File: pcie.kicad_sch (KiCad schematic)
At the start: 3 parts, among them U3002 XC7K160T-FFG676

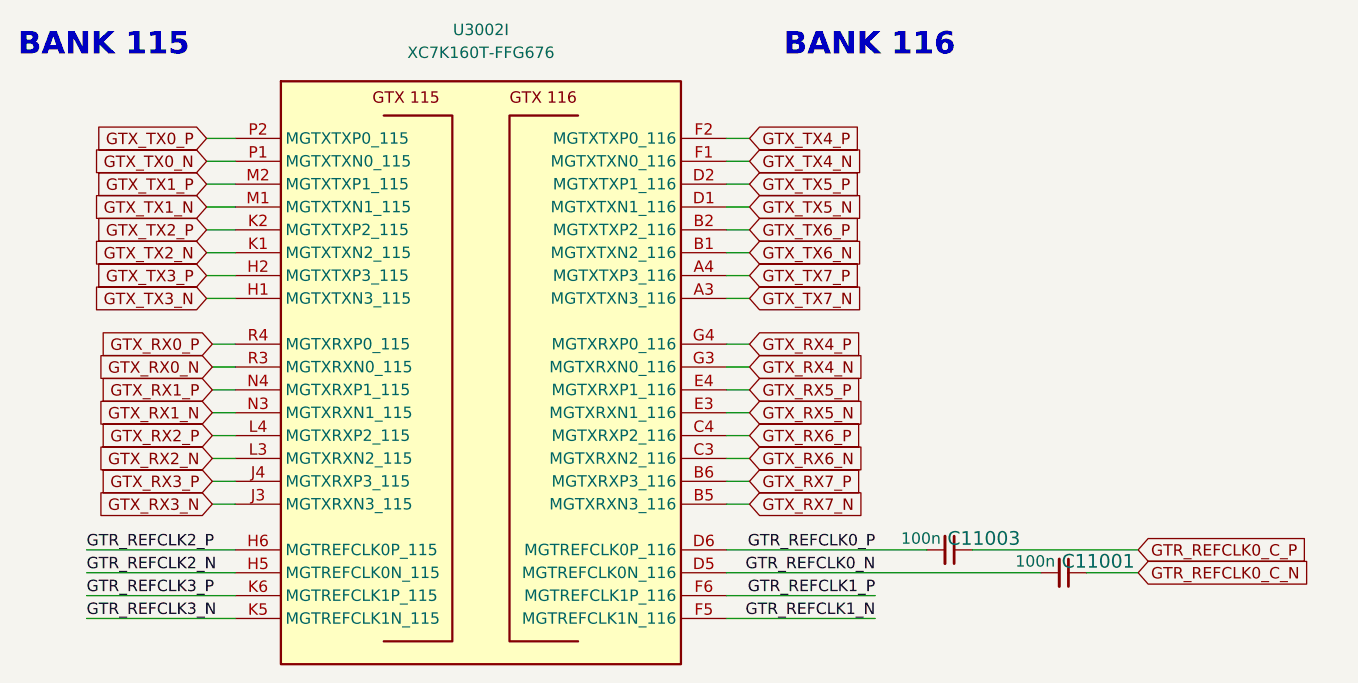
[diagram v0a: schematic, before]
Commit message: Re-annotate schematic
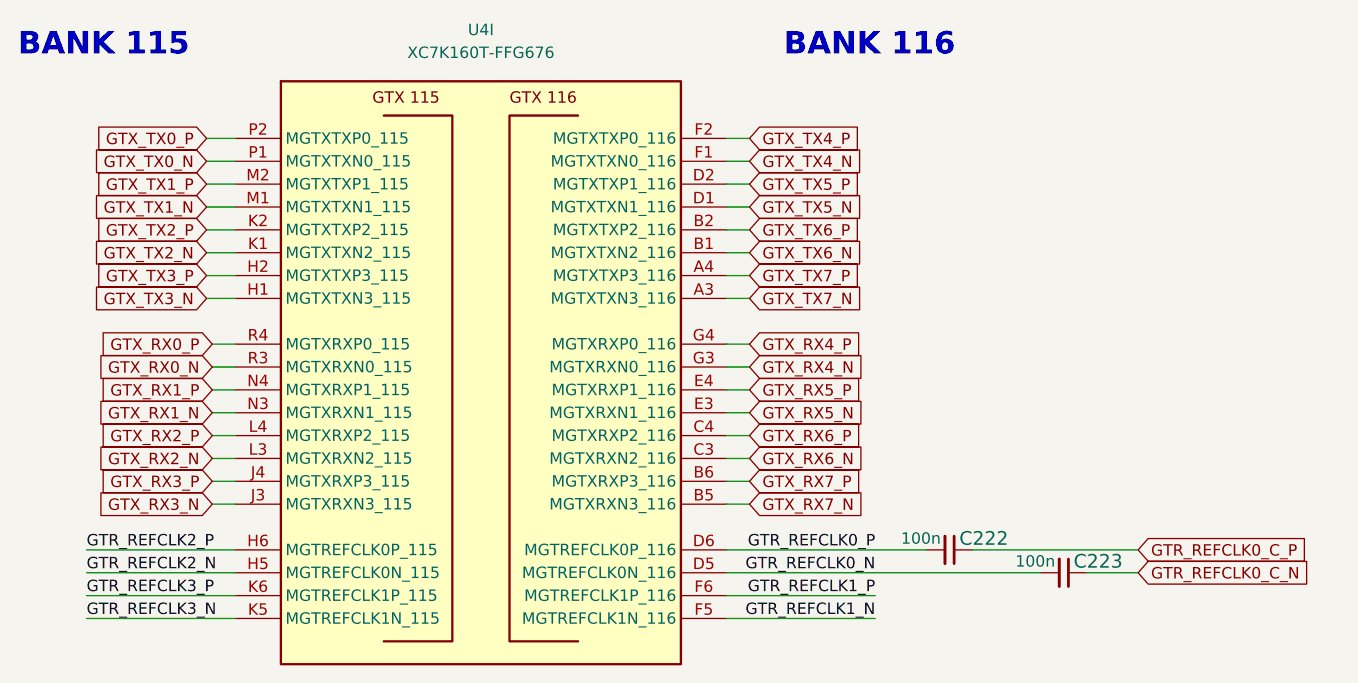
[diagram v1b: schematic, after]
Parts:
- renumbered C11003 to C222, C11001 to C223, U3002 to U4
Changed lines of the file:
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@@
   (symbol (lib_id "sodimm-ddr5-tester:C_100n_0402") (at 254 99.06 0) (mirror y) (unit 1)
     (in_bom yes) (on_board yes)
-    (property "Reference" "C11003" (id 0) (at 255.27 97.79 0)
+    (property "Reference" "C222" (id 0) (at 255.27 97.79 0)
       (effects (font (size 1.524 1.524)))
     )
@@
   (symbol (lib_id "sodimm-ddr5-tester:XC7K160T-FFG676") (at 172.085 53.34 0) (unit 9)
     (in_bom yes) (on_board yes) (fields_autoplaced)
-    (property "Reference" "U3002" (id 0) (at 199.39 41.275 0))
+    (property "Reference" "U4" (id 0) (at 199.39 41.275 0))
     (property "Value" "XC7K160T-FFG676" (id 1) (at 199.39 43.815 0)
       (effects (font (size 1.27 1.27) (thickness 0.15)))
@@
   (symbol (lib_id "sodimm-ddr5-tester:C_100n_0402") (at 266.7 101.6 0) (mirror y) (unit 1)
     (in_bom yes) (on_board yes)
-    (property "Reference" "C11001" (id 0) (at 267.97 100.33 0)
+    (property "Reference" "C223" (id 0) (at 267.97 100.33 0)
       (effects (font (size 1.524 1.524)))
     )

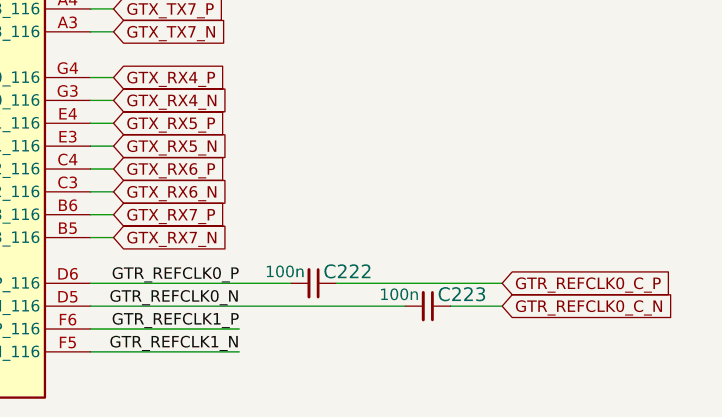
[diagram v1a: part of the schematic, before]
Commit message: Connect DDR hierarchical labels. Define and connect JTAG, RGMII, TDMS, UART, and SDIO buses. Reorganize schematic blocks between sheets
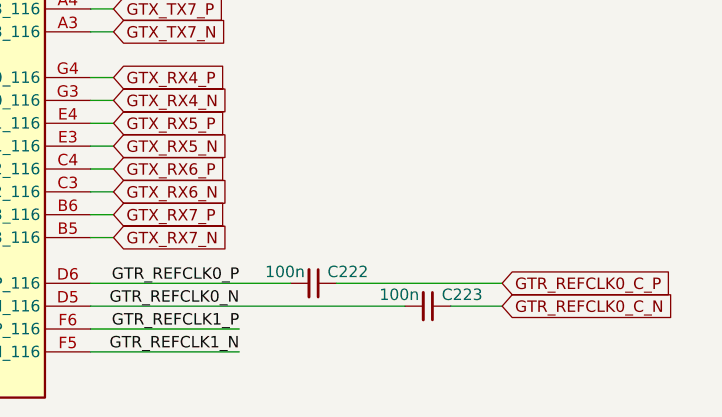
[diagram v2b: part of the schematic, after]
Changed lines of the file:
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@@
   (symbol (lib_id "sodimm-ddr5-tester:C_100n_0402") (at 254 99.06 0) (mirror y) (unit 1)
     (in_bom yes) (on_board yes)
-    (property "Reference" "C222" (id 0) (at 255.27 97.79 0)
-      (effects (font (size 1.524 1.524)))
-    )
+    (property "Reference" "C222" (id 0) (at 255.27 97.79 0))
     (property "Value" "C_100n_0402" (id 1) (at 233.68 109.22 0)
       (effects (font (size 1.27 1.27) (thickness 0.15)) (justify left bottom) hide)
@@
   (symbol (lib_id "sodimm-ddr5-tester:C_100n_0402") (at 266.7 101.6 0) (mirror y) (unit 1)
     (in_bom yes) (on_board yes)
-    (property "Reference" "C223" (id 0) (at 267.97 100.33 0)
-      (effects (font (size 1.524 1.524)))
-    )
+    (property "Reference" "C223" (id 0) (at 267.97 100.33 0))
     (property "Value" "C_100n_0402" (id 1) (at 246.38 111.76 0)
       (effects (font (size 1.27 1.27) (thickness 0.15)) (justify left bottom) hide)
